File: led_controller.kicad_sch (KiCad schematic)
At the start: 9 parts, among them M1 3V/6V/12V

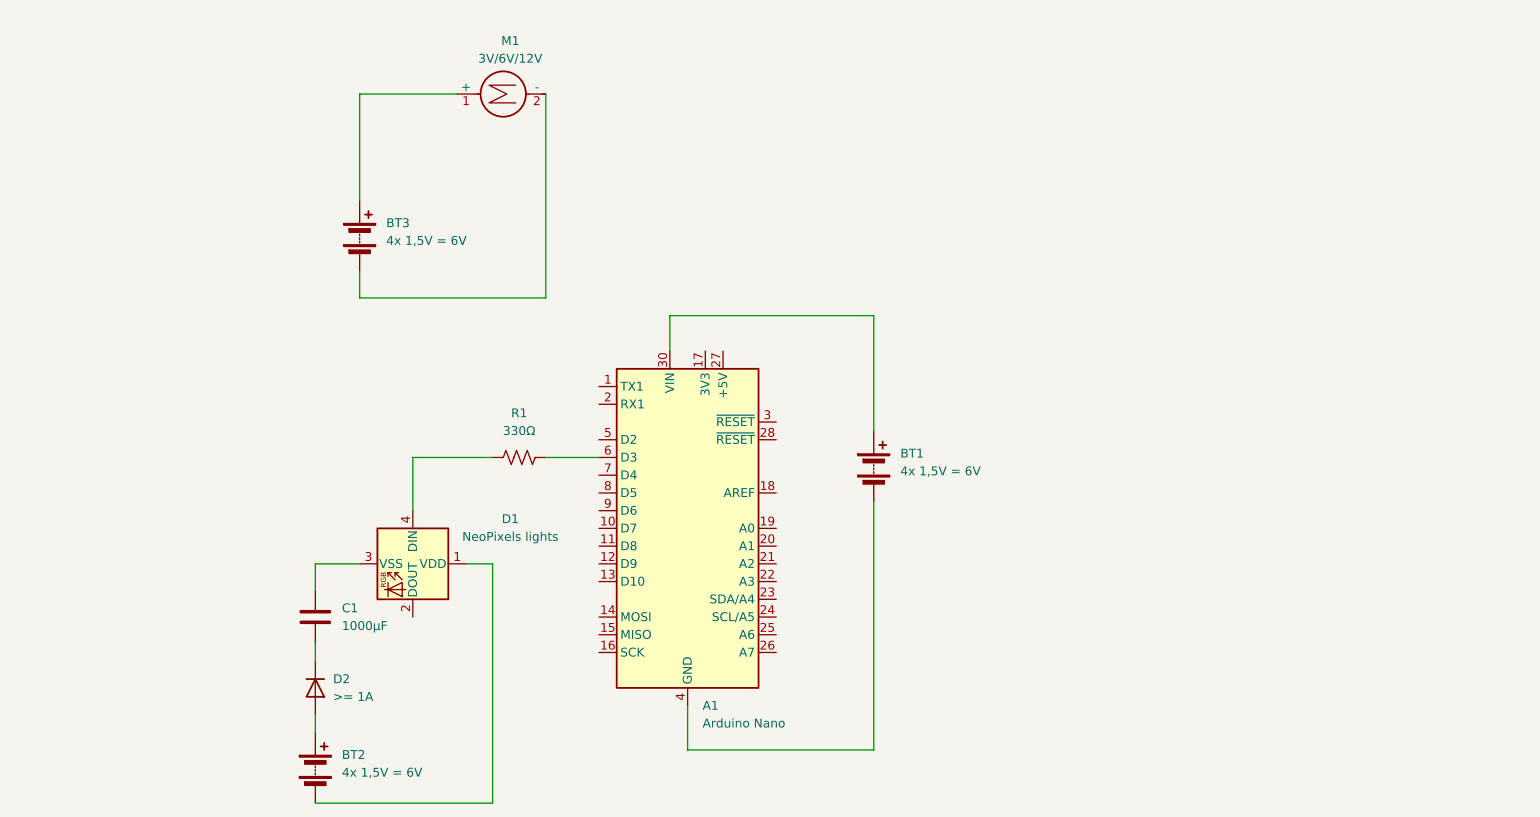
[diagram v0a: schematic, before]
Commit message: convert to one usb battery
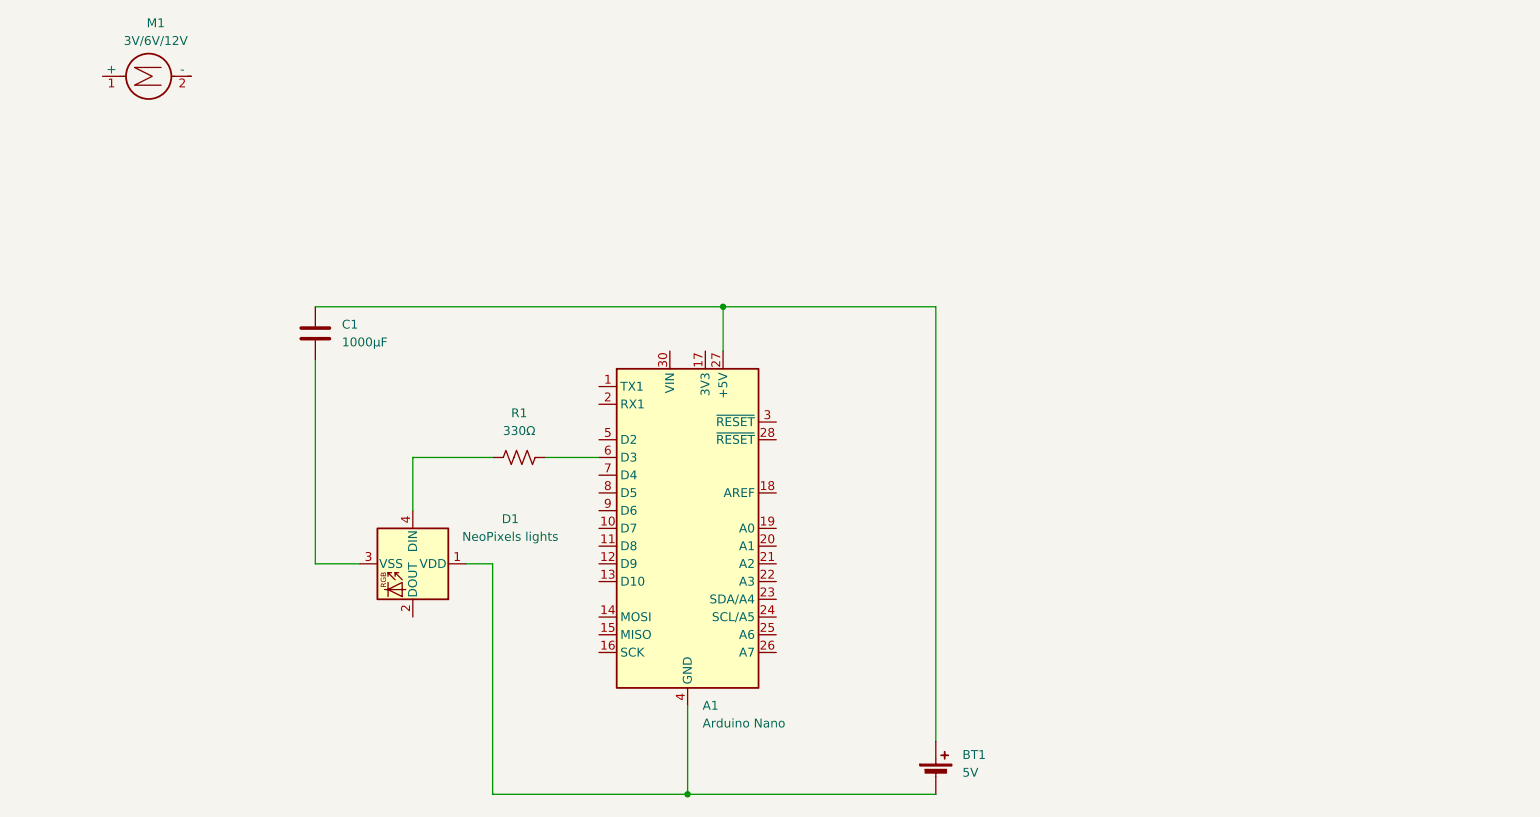
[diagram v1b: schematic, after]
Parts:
- removed BT1, BT2, BT3: 4x 1,5V = 6V, symbol Device:Battery
- removed D2: >= 1A, Diode_THT:D_DO-41_SOD81_P10.16mm_Horizontal, symbol Diode:1N4001
- added BT1: 5V, symbol Device:Battery_Cell
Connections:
- net at C1.2: now also A1.27 (+5V), BT1.1 (+)
- net at D1.1 (VDD): now also A1.29 (GND), A1.4 (GND), BT1.2 (-)
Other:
- moved on the sheet: C1, M1

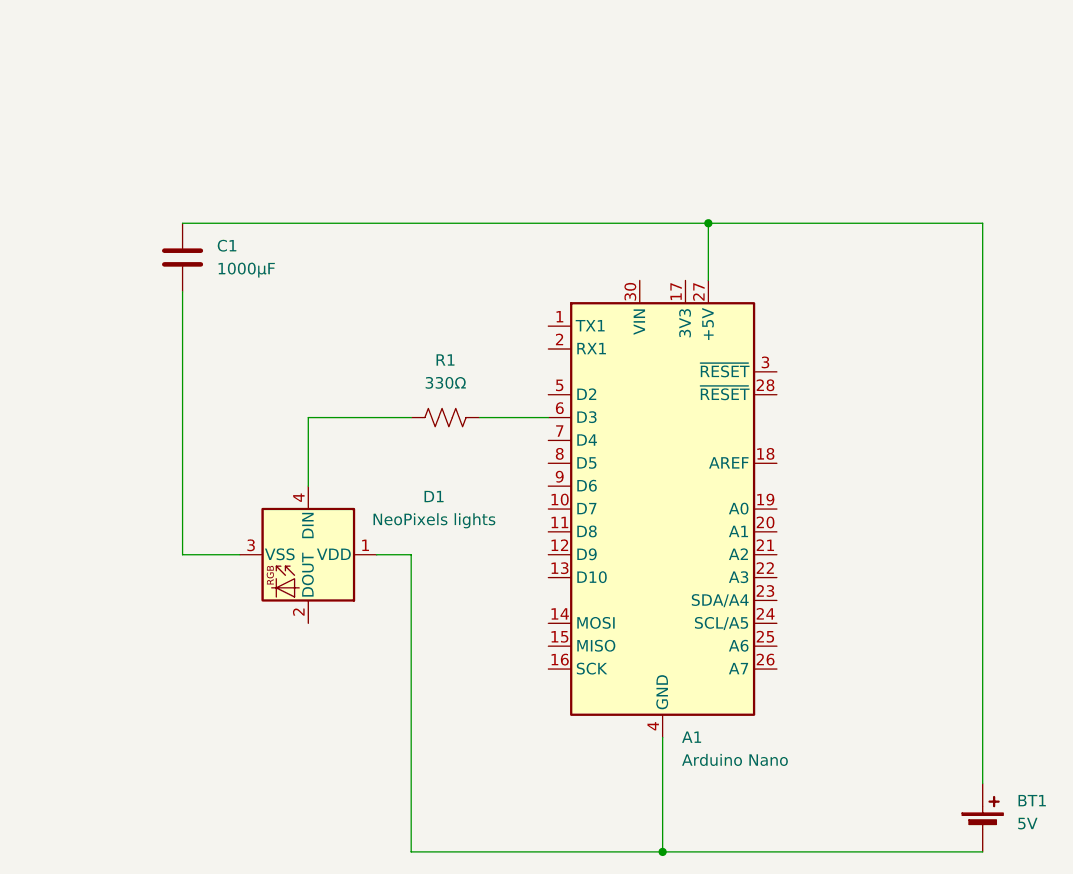
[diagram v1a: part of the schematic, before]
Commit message: add 1000 microF capacitor and 0,1 microF capacitors
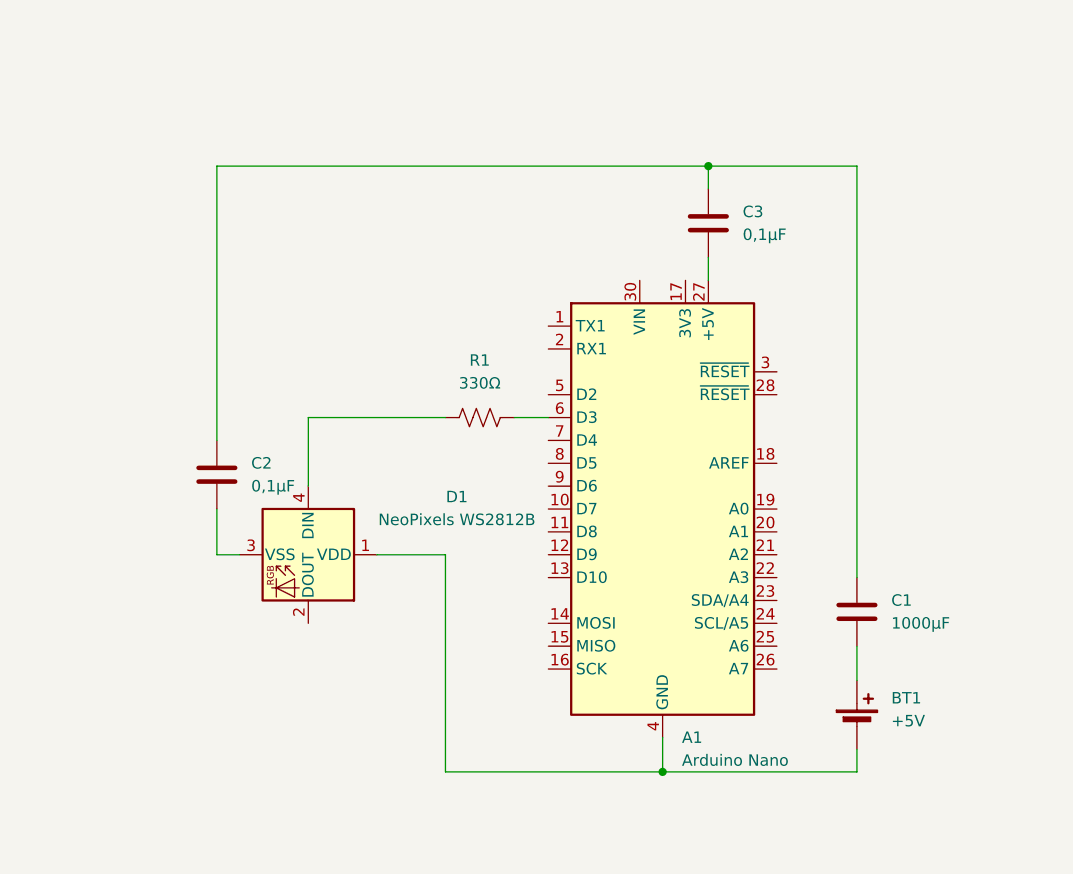
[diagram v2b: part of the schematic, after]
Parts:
- added C2, C3: 0,1µF, symbol Device:C
- BT1: value 5V -> +5V
- D1: value NeoPixels lights -> NeoPixels WS2812B
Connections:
- net at D1.3 (VSS): now also C2.2; no longer C1.1
- new net: C1.2, C2.1, C3.1
- new net: BT1.1 (+), C1.1
- new net: A1.27 (+5V), C3.2
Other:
- moved on the sheet: BT1, C1, R1

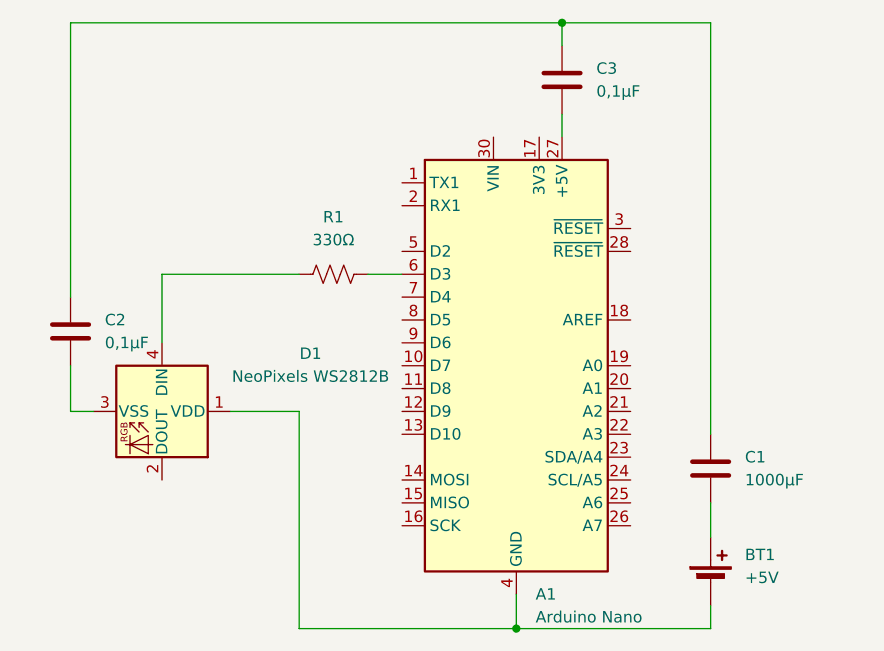
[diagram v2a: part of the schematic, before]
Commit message: change arduino version to the actual one
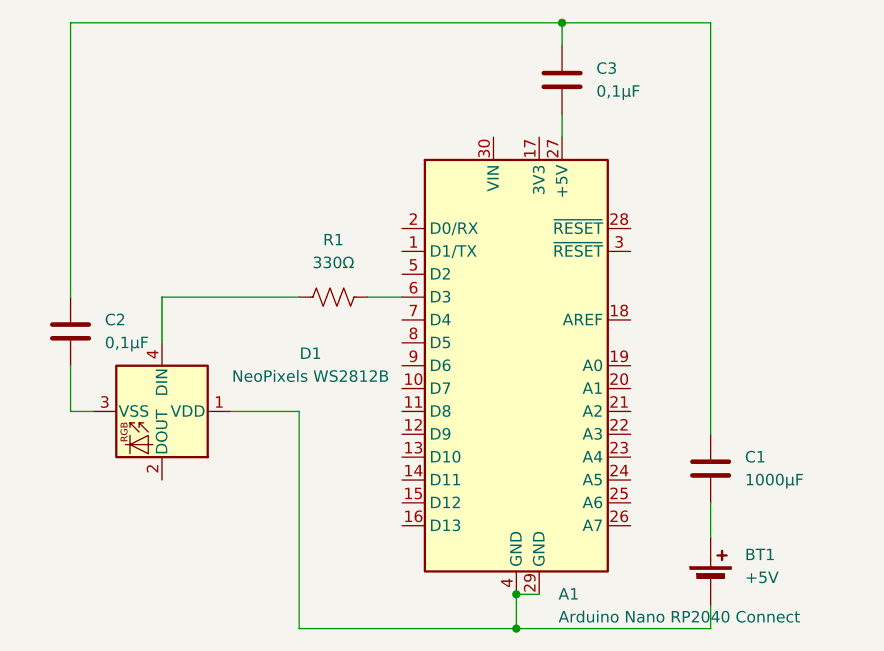
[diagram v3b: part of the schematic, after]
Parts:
- removed A1: Arduino Nano, Module:Arduino_Nano, symbol MCU_Module:Arduino_Nano_Every
- added A1: Arduino Nano RP2040 Connect, Module:Arduino_Nano, symbol MCU_Module:Arduino_Nano_v2.x
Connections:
- net at BT1.2 (-), D1.1 (VDD): now also A1.29 (GND), A1.4 (GND)
- net at R1.2: now also A1.6 (D3)
- net at C3.2: now also A1.27 (+5V)
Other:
- moved on the sheet: R1
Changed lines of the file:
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@@
+	)
+	(junction
+		(at 153.67 120.65)
+		(diameter 0)
+		(color 0 0 0 0)
 	)
 	(junction
@@
 	(wire
 		(pts
-			(xy 114.3 85.09) (xy 114.3 92.71)
+			(xy 114.3 87.63) (xy 114.3 92.71)
+		)
+		(stroke
+			(width 0)
+			(type default)
+		)
+	)
+	(wire
+		(pts
+			(xy 153.67 120.65) (xy 156.21 120.65)
 		)
 		(stroke
@@
 	(wire
 		(pts
-			(xy 129.54 85.09) (xy 114.3 85.09)
+			(xy 129.54 87.63) (xy 114.3 87.63)
 		)
 		(stroke
@@
 	(wire
 		(pts
-			(xy 137.16 85.09) (xy 140.97 85.09)
+			(xy 137.16 87.63) (xy 140.97 87.63)
 		)
 		(stroke
@@
 	(symbol
 		(lib_id "Device:R_US")
-		(at 133.35 85.09 90)
+		(at 133.35 87.63 90)
 		(unit 1)
 		(exclude_from_sim no)
@@
 		(fields_autoplaced yes)
 		(property "Reference" "R1"
-			(at 133.35 78.74 90)
+			(at 133.35 81.28 90)
 			(effects
 				(font
@@
 		)
 		(property "Value" "330Ω"
-			(at 133.35 81.28 90)
+			(at 133.35 83.82 90)
 			(effects
 				(font
@@
 		)
 		(property "Footprint" ""
-			(at 133.604 84.074 90)
+			(at 133.604 86.614 90)
 			(effects
 				(font
@@
 		)
 		(property "Datasheet" "~"
-			(at 133.35 85.09 0)
+			(at 133.35 87.63 0)
 			(effects
 				(font
@@
 		)
 		(property "Description" "Resistor, US symbol"
-			(at 133.35 85.09 0)
+			(at 133.35 87.63 0)
 			(effects
 				(font
@@
 	)
 	(symbol
+		(lib_id "MCU_Module:Arduino_Nano_v2.x")
+		(at 153.67 95.25 0)
+		(unit 1)
+		(exclude_from_sim no)
+		(in_bom yes)
+		(on_board yes)
+		(dnp no)
+		(fields_autoplaced yes)
+		(property "Reference" "A1"
+			(at 158.3533 120.65 0)
+			(effects
+				(font
+					(size 1.27 1.27)
+				)
+				(justify left)
+			)
+		)
+		(property "Value" "Arduino Nano RP2040 Connect"
+			(at 158.3533 123.19 0)
+			(effects
+				(font
+					(size 1.27 1.27)
+				)
+				(justify left)
+			)
+		)
+		(property "Footprint" "Module:Arduino_Nano"
+			(at 153.67 95.25 0)
+			(effects
+				(font
+					(size 1.27 1.27)
+					(italic yes)
+				)
+				(hide yes)
+			)
+		)
+		(property "Datasheet" "https://www.arduino.cc/en/uploads/Main/ArduinoNanoManual23.pdf"
+			(at 153.67 95.25 0)
+			(effects
+				(font
+					(size 1.27 1.27)
+				)
+				(hide yes)
+			)
+		)
+		(property "Description" "Arduino Nano v2.x"
+			(at 153.67 95.25 0)
+			(effects
+				(font
+					(size 1.27 1.27)
+				)
+				(hide yes)
+			)
+		)
+		(pin "13"
+		)
+		(pin "9"
+		)
+		(pin "8"
+		)
+		(pin "5"
+		)
+		(pin "6"
+		)
+		(pin "12"
+		)
+		(pin "7"
+		)
+		(pin "10"
+		)
+		(pin "23"
+		)
+		(pin "18"
+		)
+		(pin "15"
+		)
+		(pin "2"
+		)
+		(pin "1"
+		)
+		(pin "11"
+		)
+		(pin "30"
+		)
+		(pin "4"
+		)
+		(pin "3"
+		)
+		(pin "21"
+		)
+		(pin "16"
+		)
+		(pin "28"
+		)
+		(pin "14"
+		)
+		(pin "29"
+		)
+		(pin "27"
+		)
+		(pin "19"
+		)
+		(pin "20"
+		)
+		(pin "17"
+		)
+		(pin "22"
+		)
+		(pin "24"
+		)
+		(pin "25"
+		)
+		(pin "26"
+		)
+		(instances
+			(project ""
+				(path "/33db064c-d5ae-416f-86c1-c095f962d498"
+					(reference "A1")
+					(unit 1)
+				)
+			)
+		)
+	)
+	(symbol
 		(lib_id "Device:C")
 		(at 175.26 106.68 180)
@@
 					(unit 1)
 				)
-			)
-		)
-	)
-	(symbol
-		(lib_id "MCU_Module:Arduino_Nano_Every")
-		(at 153.67 95.25 0)
-		(unit 1)
-		(exclude_from_sim no)
-		(in_bom yes)
-		(on_board yes)
-		(dnp no)
-		(fields_autoplaced yes)
-		(property "Reference" "A1"
-			(at 155.8133 120.65 0)
-			(effects
-				(font
-					(size 1.27 1.27)
-				)
-				(justify left)
-			)
-		)
-		(property "Value" "Arduino Nano"
-			(at 155.8133 123.19 0)
-			(effects
-				(font
-					(size 1.27 1.27)
-				)
-				(justify left)
-			)
-		)
-		(property "Footprint" "Module:Arduino_Nano"
-			(at 153.67 95.25 0)
-			(effects
-				(font
-					(size 1.27 1.27)
-					(italic yes)
-				)
-				(hide yes)
-			)
-		)
-		(property "Datasheet" "https://content.arduino.cc/assets/NANOEveryV3.0_sch.pdf"
-			(at 153.67 95.25 0)
-			(effects
-				(font
-					(size 1.27 1.27)
-				)
-				(hide yes)
-			)
-		)
-		(property "Description" "Arduino Nano Every"
-			(at 153.67 95.25 0)
-			(effects
-				(font
-					(size 1.27 1.27)
-				)
-				(hide yes)
-			)
-		)
-		(pin "10"
-		)
-		(pin "4"
-		)
-		(pin "5"
-		)
-		(pin "19"
-		)
-		(pin "28"
-		)
-		(pin "22"
-		)
-		(pin "24"
-		)
-		(pin "26"
-		)
-		(pin "13"
-		)
-		(pin "1"
-		)
-		(pin "9"
-		)
-		(pin "14"
-		)
-		(pin "29"
-		)
-		(pin "2"
-		)
-		(pin "8"
-		)
-		(pin "12"
-		)
-		(pin "15"
-		)
-		(pin "17"
-		)
-		(pin "27"
-		)
-		(pin "7"
-		)
-		(pin "6"
-		)
-		(pin "11"
-		)
-		(pin "16"
-		)
-		(pin "30"
-		)
-		(pin "3"
-		)
-		(pin "18"
-		)
-		(pin "20"
-		)
-		(pin "21"
-		)
-		(pin "23"
-		)
-		(pin "25"
-		)
-		(instances
-			(project ""
-				(path "/33db064c-d5ae-416f-86c1-c095f962d498"
-					(reference "A1")
-					(unit 1)
-				)
